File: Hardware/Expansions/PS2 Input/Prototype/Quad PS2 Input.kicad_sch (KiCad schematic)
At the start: 23 parts, among them J101 Conn_02x06_Counter_Clockwise, J102 Mini-DIN-6, J103 Mini-DIN-6, J104 Mini-DIN-6, J105 Mini-DIN-6, J106 LVLSHIFT, J107 LVLSHIFT, J108 QWIIC, U101 24LC64

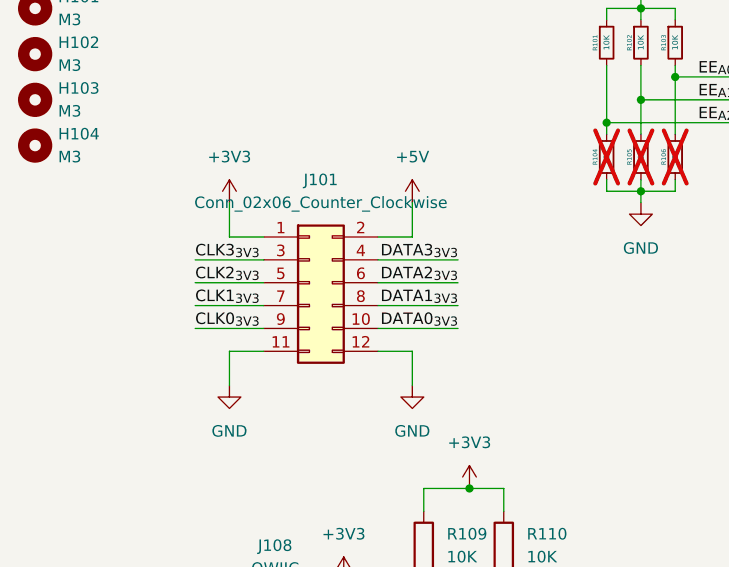
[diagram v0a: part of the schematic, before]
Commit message: Fixes PS/2 input code for new prototype PCB, adds program.py to flash EEPROM
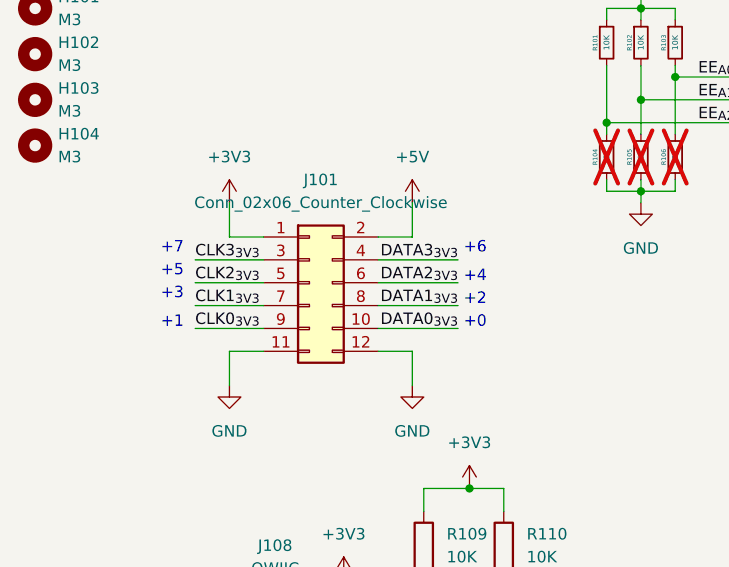
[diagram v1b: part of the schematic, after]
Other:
- note added: "+0"
- note added: "+1"
- note added: "+2"
- note added: "+3"
- note added: "+4"
- note added: "+5"
- note added: "+6"
- note added: "+7"
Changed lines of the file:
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@@
 	(generator_version "9.0")
 	(paper "A4")
+	(text "+1"
+		(exclude_from_sim no)
+		(at 40.64 60.325 0)
+		(effects
+			(font
+				(size 1.27 1.27)
+			)
+		)
+	)
+	(text "+3"
+		(exclude_from_sim no)
+		(at 40.64 57.15 0)
+		(effects
+			(font
+				(size 1.27 1.27)
+			)
+		)
+	)
+	(text "+0"
+		(exclude_from_sim no)
+		(at 74.295 60.325 0)
+		(effects
+			(font
+				(size 1.27 1.27)
+			)
+		)
+	)
+	(text "+5"
+		(exclude_from_sim no)
+		(at 40.64 54.61 0)
+		(effects
+			(font
+				(size 1.27 1.27)
+			)
+		)
+	)
+	(text "+7"
+		(exclude_from_sim no)
+		(at 40.64 52.07 0)
+		(effects
+			(font
+				(size 1.27 1.27)
+			)
+		)
+	)
+	(text "+6"
+		(exclude_from_sim no)
+		(at 74.295 52.07 0)
+		(effects
+			(font
+				(size 1.27 1.27)
+			)
+		)
+	)
+	(text "+4"
+		(exclude_from_sim no)
+		(at 74.295 55.245 0)
+		(effects
+			(font
+				(size 1.27 1.27)
+			)
+		)
+	)
+	(text "+2"
+		(exclude_from_sim no)
+		(at 74.295 57.785 0)
+		(effects
+			(font
+				(size 1.27 1.27)
+			)
+		)
+	)
 	(junction
 		(at 88.9 38.1)
